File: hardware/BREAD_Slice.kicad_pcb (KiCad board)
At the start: 2 copper layers, 70 x 100 mm, 24 parts, among them J1 I2C_01x04, J2 Conn_01x10_Female, J3 Term_2, J4 Term_2, Q1 TIP120

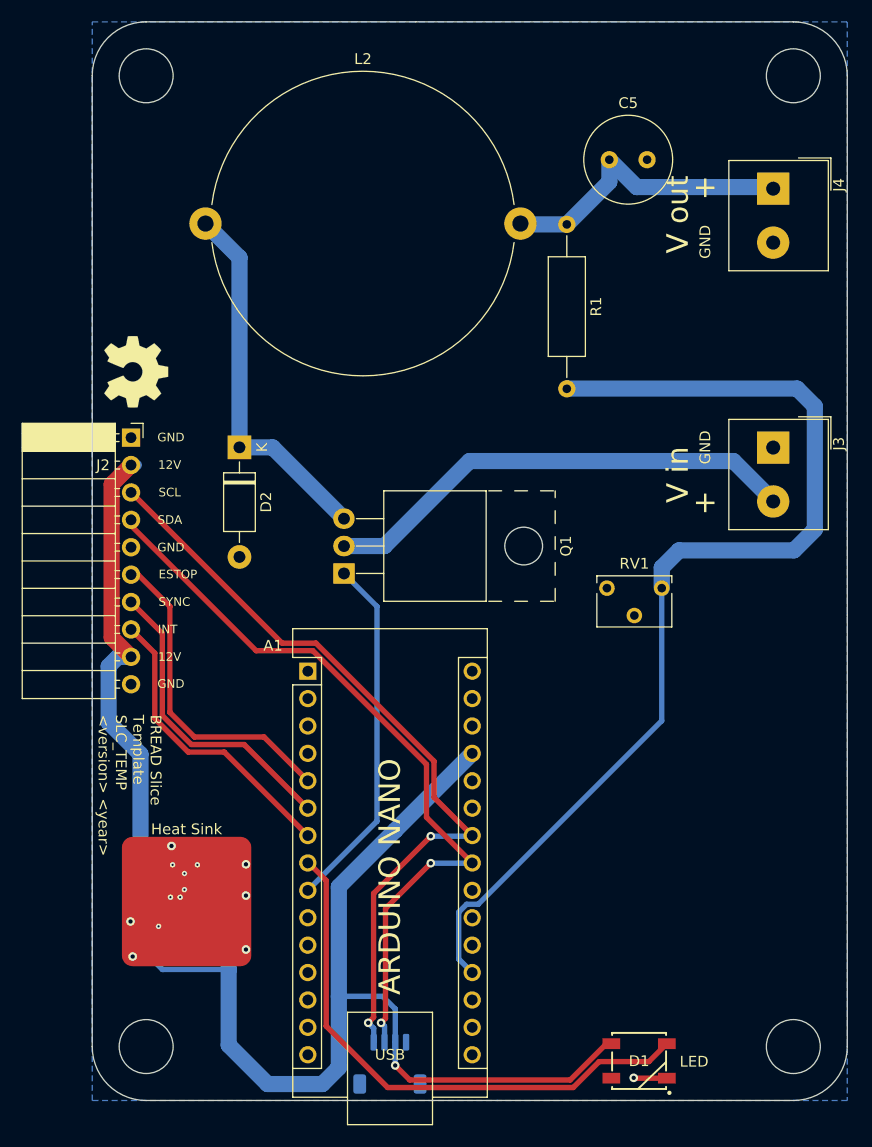
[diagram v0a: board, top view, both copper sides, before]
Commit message: cleaned up erc & drc
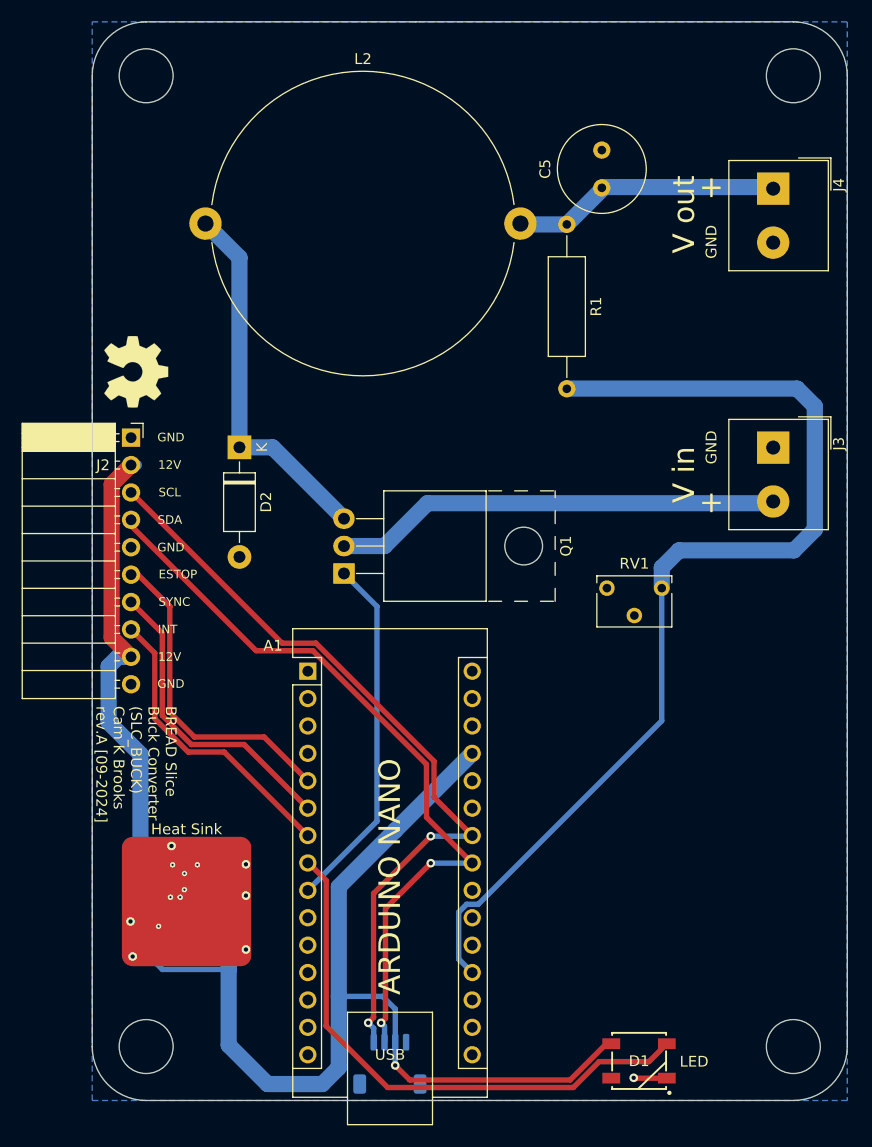
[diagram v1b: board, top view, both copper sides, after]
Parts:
- moved C5 2.70 mm to (169.8, 55.2), turned to 90 degrees
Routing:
- net Net-(C5-Pad1): track 28.3 -> 24.9 mm
- net Net-(Q1-C): track 44.6 -> 41.6 mm
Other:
- board text added: "BREAD Slice Buck Converter (SLC_BUCK) Cam K Brooks rev.A [09-2024]"
- board text removed: "BREAD Slice Template SLC_TEMP <version> <year>"
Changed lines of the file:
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@@
 	(footprint "Capacitor_THT:C_Radial_D8.0mm_H11.5mm_P3.50mm"
 		(layer "F.Cu")
-		(at 170.54 52.58)
+		(at 169.844 55.19 90)
 		(descr "C, Radial series, Radial, pin pitch=3.50mm, diameter=8mm, height=11.5mm, Non-Polar Electrolytic Capacitor")
 		(tags "C Radial series Radial pin pitch 3.50mm diameter 8mm height 11.5mm Non-Polar Electrolytic Capacitor")
 		(property "Reference" "C5"
-			(at 1.75 -5.25 0)
+			(at 1.75 -5.25 90)
 			(layer "F.SilkS")
 			(effects
@@
 		)
 		(property "Value" "100uF"
-			(at 1.75 5.25 0)
+			(at 1.75 5.25 90)
 			(layer "F.Fab")
 			(effects
@@
 		)
 		(property "Footprint" "Capacitor_THT:C_Radial_D8.0mm_H11.5mm_P3.50mm"
-			(at 0 0 0)
+			(at 0 0 90)
 			(unlocked yes)
 			(layer "F.Fab")
@@
 		)
 		(property "Datasheet" ""
-			(at 0 0 0)
+			(at 0 0 90)
 			(unlocked yes)
 			(layer "F.Fab")
@@
 		)
 		(property "Description" ""
-			(at 0 0 0)
+			(at 0 0 90)
 			(unlocked yes)
 			(layer "F.Fab")
@@
 		)
 		(fp_text user "${REFERENCE}"
-			(at 1.75 0 0)
+			(at 1.75 0 90)
 			(layer "F.Fab")
 			(effects
@@
 		)
 		(pad "1" thru_hole circle
-			(at 0 0)
+			(at 0 0 90)
 			(size 1.6 1.6)
 			(drill 0.8)
@@
 		)
 		(pad "2" thru_hole circle
-			(at 3.5 0)
+			(at 3.5 0 90)
 			(size 1.6 1.6)
 			(drill 0.8)
@@
 	)
 	(gr_text "V in"
-		(at 176.89 81.79 90)
+		(at 177.464 81.79 90)
 		(layer "F.SilkS")
 		(effects
@@
 	)
 	(gr_text "V out"
-		(at 176.89 57.66 90)
+		(at 177.464 57.66 90)
 		(layer "F.SilkS")
 		(effects
@@
 	)
 	(gr_text "+"
-		(at 179.43 55.12 0)
+		(at 180.004 55.12 0)
 		(layer "F.SilkS")
 		(effects
@@
 		)
 	)
-	(gr_text "BREAD Slice\nTemplate\nSLC_TEMP\n<version> <year>"
-		(at 126.066 104.035 270)
+	(gr_text "BREAD Slice\nBuck Converter\n(SLC_BUCK)\nCam K Brooks\nrev.A [09-2024]"
+		(at 126.664 103.224 270)
 		(layer "F.SilkS")
 		(effects
@@
 	)
 	(gr_text "GND"
-		(at 179.43 60.2 90)
+		(at 180.004 60.2 90)
 		(layer "F.SilkS")
 		(effects
@@
 	)
 	(gr_text "GND"
-		(at 179.43 79.25 90)
+		(at 180.004 79.25 90)
 		(layer "F.SilkS")
 		(effects
@@
 	)
 	(gr_text "+"
-		(at 179.43 84.33 0)
+		(at 180.004 84.33 0)
 		(layer "F.SilkS")
 		(effects
@@
 	)
 	(segment
-		(start 173.08 55.12)
-		(end 170.54 52.58)
-		(width 1.5)
-		(layer "B.Cu")
-		(net 34)
-	)
-	(segment
 		(start 166.6 58.58)
 		(end 162.38 58.58)
@@
 	)
 	(segment
-		(start 170.54 52.58)
-		(end 170.54 54.64)
+		(start 170.06 55.12)
+		(end 166.6 58.58)
 		(width 1.5)
 		(layer "B.Cu")
@@
 	)
 	(segment
-		(start 170.54 54.64)
-		(end 166.6 58.58)
+		(start 173.08 55.12)
+		(end 170.06 55.12)
 		(width 1.5)
 		(layer "B.Cu")
@@
 	)
 	(segment
-		(start 185.78 84.25)
-		(end 182.05 80.52)
-		(width 1.5)
-		(layer "B.Cu")
-		(net 36)
-	)
-	(segment
-		(start 149.6 88.4)
-		(end 145.94 88.4)
+		(start 153.672 84.428)
+		(end 149.7 88.4)
 		(width 1.5)
 		(layer "B.Cu")
@@
 	)
 	(segment
-		(start 157.58 80.52)
-		(end 149.7 88.4)
+		(start 185.602 84.428)
+		(end 153.672 84.428)
 		(width 1.5)
 		(layer "B.Cu")
@@
 	(segment
 		(start 149.7 88.4)
-		(end 149.6 88.4)
+		(end 145.94 88.4)
 		(width 1.5)
 		(layer "B.Cu")
@@
 	)
 	(segment
-		(start 182.05 80.52)
-		(end 157.58 80.52)
+		(start 185.78 84.25)
+		(end 185.602 84.428)
 		(width 1.5)
 		(layer "B.Cu")
